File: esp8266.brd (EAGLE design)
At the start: 29.5 x 28.6 mm, 31 parts, among them U1 FT232RL-BASICSSOP, U2 SPX3819M5-L33, U3 SPX3819M5-L33

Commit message: Some board updates
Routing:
- net VIN: track 74.8 -> 75.7 mm

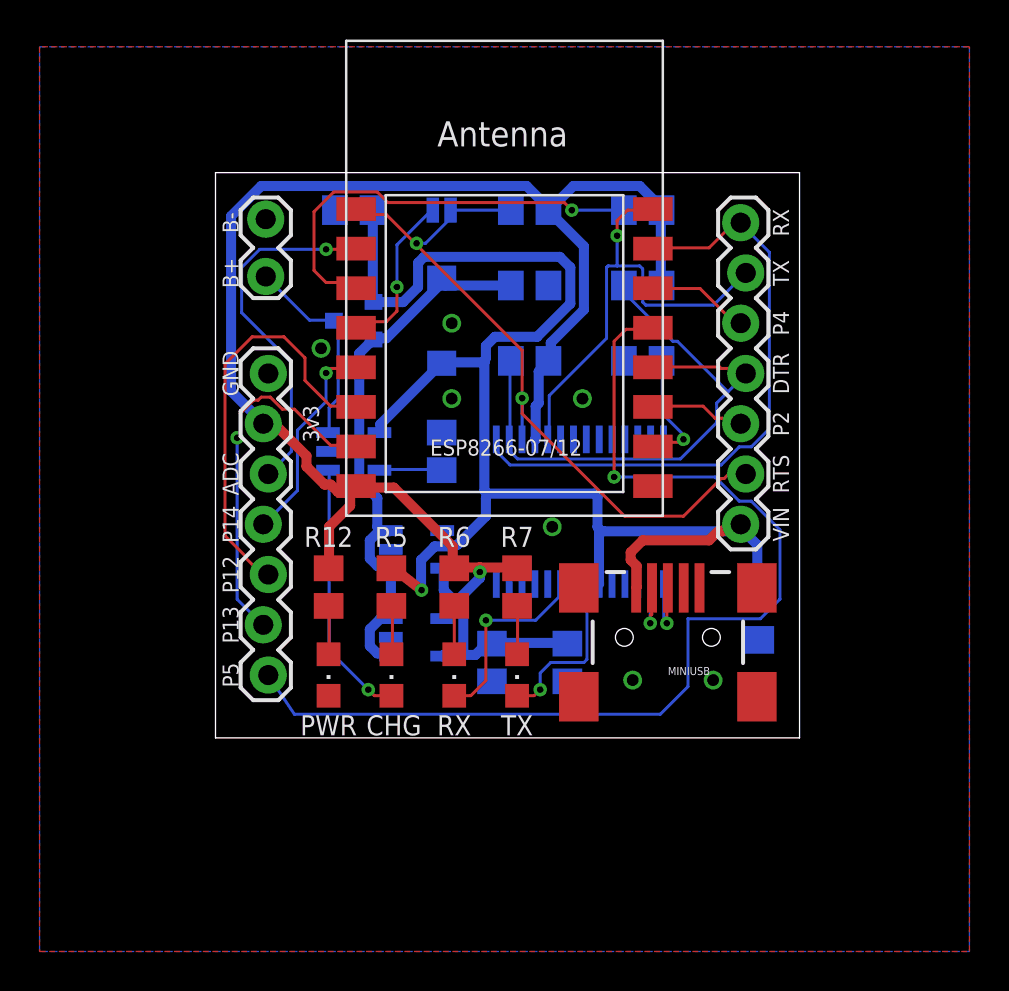
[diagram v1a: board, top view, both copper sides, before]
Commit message: Minor fixes and improvements.
Watchdog with pull ups and a AND Gate;
Diode after VIN for satefy reasons;
Additional VIN pin on the other side of the board for completeness;
Switched order of pins 13 and 12;
Small border test holes for VIN and GND.
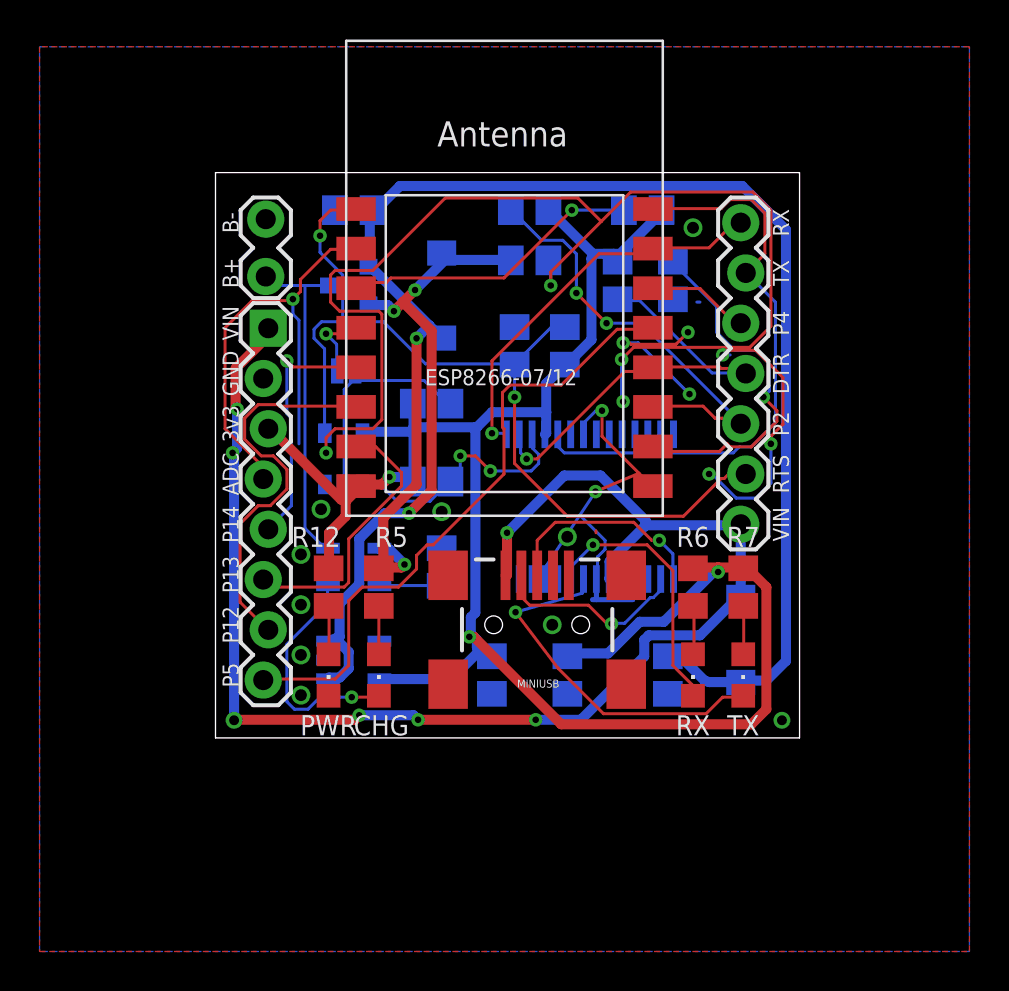
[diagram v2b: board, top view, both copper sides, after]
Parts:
- removed JP4: (no value), SparkFun-Connectors:1X07_LOCK
- removed U3: SPX3819M5-L33, SparkFun-PowerIC:SOT23-5
- added C5: 470pF, rcl:C0805
- added D1: 1N5817, SparkFun-DiscreteSemi:SMA-DIODE
- added IC1: 74LVC1G08DBV, 74xx-little-us:SOT23-5
- added JP1: (no value), SparkFun-Connectors:1X08_LOCK
- added R10, R3: 10k, resistor:R0805
- C2: value 2.2uF -> 4.7uF
- C4: value (none) -> 10uF; device SparkFun-Capacitors:EIA3216 -> rcl:C0805
- moved R6 12.1 mm to (33.0, 59.1)
- moved RX 12.1 mm to (33.0, 54.6)
- moved R7 11.4 mm to (35.6, 59.1)
- moved TX 11.4 mm to (35.6, 54.6)
- moved RST-P16 9.45 mm to (15.5, 70.0)
- moved MINIUSB 6.63 mm to (25.1, 57.1)
- moved U2 6.43 mm to (15.9, 55.4)
- moved MCP73831 5.84 mm to (15.9, 60.1)
- moved R13 5.84 mm to (20.3, 60.1)
- moved C4 5.57 mm to (31.8, 54.6), turned to 270 degrees
- moved R4 4.34 mm to (32.0, 74.5), turned to 270 degrees
- moved R1 1.93 mm to (26.5, 71.2), turned to 90 degrees
- moved U$1 1.80 mm to (15.6, 74.3)
- moved R9 1.30 mm to (29.2, 74.5), turned to 270 degrees
- moved D2 1.27 mm to (20.3, 73.8)
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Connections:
- new net FTDI_RTS: IC1.1, R10.1, U1.3
- new net N$2: C4.1, D1.C, D2.A, MCP73831.4, R12.1, R14.1, U$1.1
- new net N$4: IC1.2, R3.1, RST-P16.1
- net 3V3: now also IC1.5, JP1.3, R10.2, R3.2; no longer JP4.2, U3.5
- net ADC: now also JP1.4; no longer JP4.3
- net DTR: no longer R1.2
- net GND: now also C4.2, C5.2, IC1.3, JP1.2; no longer C4.C, JP4.1, U3.2
- net P12: now also JP1.7; no longer JP4.5
- net P13: now also JP1.6; no longer JP4.6
- net P14: now also JP1.5; no longer JP4.4
- net P2: now also R8.2
- net P5: now also JP1.8; no longer JP4.7
- net RTS: now also C5.1, IC1.4, R1.2; no longer R8.2, RST-P16.1, U1.3
- net VIN: now also D1.A, JP1.1; no longer C4.A, D2.A, MCP73831.4, R12.1, R14.1, U$1.1
- net VRIN: no longer U3.1, U3.3
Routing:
- net GND: track 0.00 -> 105.3 mm, vias 7 -> 22
- net N$2: track 0.00 -> 75.5 mm, vias 0 -> 2
- net P5: track 53.4 -> 31.9 mm, vias 1 -> 0
- net P2: track 4.86 -> 22.1 mm, vias 0 -> 2
- net FTDI_RTS: track 0.00 -> 12.8 mm, vias 0 -> 2
- net 3V3: track 88.0 -> 100.6 mm, vias 1 -> 3
- net P15: track 6.16 -> 18.2 mm
- net N$4: track 0.00 -> 11.8 mm
- net RX: track 31.5 -> 20.4 mm, vias 0 -> 1
- net RXLED: track 8.91 -> 18.5 mm
- net RTS: track 36.8 -> 46.3 mm
- net DTR: track 31.7 -> 22.6 mm, vias 0 -> 1
- net D+: track 3.88 -> 10.9 mm
- net D-: track 3.82 -> 10.8 mm
- net VBAT: track 10.3 -> 17.2 mm
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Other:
- board text added: "2015.HSF+LF"
- board text removed: "2015 HSF"
